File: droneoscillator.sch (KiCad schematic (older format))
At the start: 46 parts, among them J1 Conn_01x02, J2 Conn_01x03, Q1 BC337, Q2 BC337, Q3 BC337, Q4 BC337, U1 NE5532

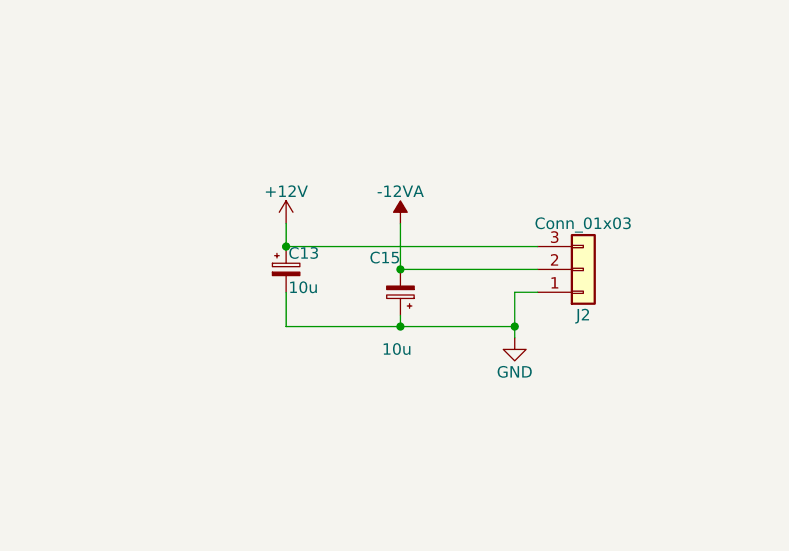
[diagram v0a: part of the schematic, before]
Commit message: added input filtering to power supply
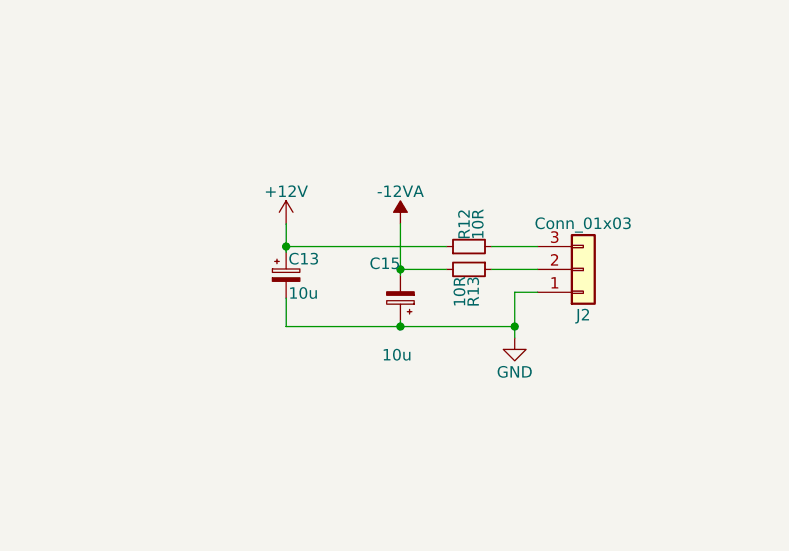
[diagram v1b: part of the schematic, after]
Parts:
- added R12, R13: 10R, Resistor_THT:R_Axial_DIN0204_L3.6mm_D1.6mm_P7.62mm_Horizontal, symbol droneoscillator-rescue:R_Small
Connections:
- net +12V: now also R12.1; no longer J2.3 (Pin_3)
- net -12VA: now also R13.2; no longer J2.2 (Pin_2)
- new net: J2.2 (Pin_2), R13.1
- new net: J2.3 (Pin_3), R12.2
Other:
- moved on the sheet: C13, C15
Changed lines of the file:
@@
 L droneoscillator-rescue:CP_Small C13
 U 1 1 5B2C205C
-P 8400 4700
-F 0 "C13" H 8410 4770 50  0000 L CNN
-F 1 "10u" H 8410 4620 50  0000 L CNN
-F 2 "Capacitor_THT:CP_Radial_D4.0mm_P2.00mm" H 8400 4700 50  0001 C CNN
-F 3 "" H 8400 4700 50  0001 C CNN
-	1    8400 4700
+P 8400 4725
+F 0 "C13" H 8410 4795 50  0000 L CNN
+F 1 "10u" H 8410 4645 50  0000 L CNN
+F 2 "Capacitor_THT:CP_Radial_D4.0mm_P2.00mm" H 8400 4725 50  0001 C CNN
+F 3 "" H 8400 4725 50  0001 C CNN
+	1    8400 4725
 	1    0    0    -1
 $EndComp
@@
 L droneoscillator-rescue:CP_Small C15
 U 1 1 5B2C2235
-P 8900 4800
-F 0 "C15" H 8900 4650 50  0000 L CNN
-F 1 "10u" H 8850 5050 50  0000 L CNN
-F 2 "Capacitor_THT:CP_Radial_D4.0mm_P2.00mm" H 8900 4800 50  0001 C CNN
-F 3 "" H 8900 4800 50  0001 C CNN
-	1    8900 4800
+P 8900 4825
+F 0 "C15" H 8900 4675 50  0000 L CNN
+F 1 "10u" H 8850 5075 50  0000 L CNN
+F 2 "Capacitor_THT:CP_Radial_D4.0mm_P2.00mm" H 8900 4825 50  0001 C CNN
+F 3 "" H 8900 4825 50  0001 C CNN
+	1    8900 4825
 	-1   0    0    1
 $EndComp
@@
 	9400 4800 9500 4800
 Wire Wire Line
-	8400 4800 8400 4950
+	8400 4825 8400 4950
 Connection ~ 9400 4950
-Connection ~ 8900 4700
-Connection ~ 8400 4600
-Wire Wire Line
-	8900 4950 8900 4900
+Wire Wire Line
+	8900 4950 8900 4925
 Connection ~ 8900 4950
 Wire Wire Line
@@
 	0    -1   -1   0
 $EndComp
-Wire Wire Line
-	8400 4600 9500 4600
-Wire Wire Line
-	8900 4700 9500 4700
+$Comp
+L droneoscillator-rescue:R_Small R12
+U 1 1 5C5321D3
+P 9200 4600
+F 0 "R12" H 9230 4620 50  0000 L CNN
+F 1 "10R" H 9230 4560 50  0000 L CNN
+F 2 "Resistor_THT:R_Axial_DIN0204_L3.6mm_D1.6mm_P7.62mm_Horizontal" H 9200 4600 50  0001 C CNN
+F 3 "" H 9200 4600 50  0001 C CNN
+	1    9200 4600
+	0    -1   -1   0
+$EndComp
+$Comp
+L droneoscillator-rescue:R_Small R13
+U 1 1 5C53254E
+P 9200 4700
+F 0 "R13" H 9230 4720 50  0000 L CNN
+F 1 "10R" H 9230 4660 50  0000 L CNN
+F 2 "Resistor_THT:R_Axial_DIN0204_L3.6mm_D1.6mm_P7.62mm_Horizontal" H 9200 4700 50  0001 C CNN
+F 3 "" H 9200 4700 50  0001 C CNN
+	1    9200 4700
+	0    1    1    0
+$EndComp
+Wire Wire Line
+	9500 4600 9300 4600
+Wire Wire Line
+	9100 4600 8400 4600
+Connection ~ 8400 4600
+Wire Wire Line
+	8400 4600 8400 4625
+Wire Wire Line
+	9300 4700 9500 4700
+Wire Wire Line
+	9100 4700 8900 4700
+Connection ~ 8900 4700
+Wire Wire Line
+	8900 4700 8900 4725
 $EndSCHEMATC

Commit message: pcb and schematic tweaks
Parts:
- RV5: value 100K -> 50K
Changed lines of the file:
@@
 P 2850 5150
 F 0 "RV5" V 2675 5150 50  0000 C CNN
-F 1 "100K" V 2750 5150 50  0000 C CNN
+F 1 "50K" V 2750 5150 50  0000 C CNN
 F 2 "Potentiometer_THT:Potentiometer_Alps_RK097_Single_Horizontal" H 2850 5150 50  0001 C CNN
 F 3 "" H 2850 5150 50  0001 C CNN
@@
 	2850 5000 2850 4950
 Wire Wire Line
-	2850 4950 3050 4950
-Wire Wire Line
-	3050 4950 3050 5150
-Wire Wire Line
-	3000 5150 3050 5150
-Wire Wire Line
 	3300 5150 3300 5250
-Connection ~ 3050 5150
 Connection ~ 3300 5150
 Wire Wire Line
@@
 Wire Wire Line
 	2650 5150 2700 5150
-Wire Wire Line
-	3050 5150 3300 5150
 Wire Wire Line
 	9450 1950 9450 2050
@@
 Wire Wire Line
 	8900 4700 8900 4725
+Connection ~ 3100 5150
+Wire Wire Line
+	3100 5150 3300 5150
+Wire Wire Line
+	3000 5150 3100 5150
+Wire Wire Line
+	2850 4950 3100 4950
+Wire Wire Line
+	3100 4950 3100 5150
 $EndSCHEMATC

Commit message: small tweaks, ready for sending to production
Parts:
- J1: value Conn_01x02 -> JST_XH_2
- J2: value Conn_01x03 -> JST_XH_3
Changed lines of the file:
@@
 U 1 1 5B23B79E
 P 2750 1750
-F 0 "RV1" H 2550 1800 50  0000 C CNN
-F 1 "50K" H 2550 1700 50  0000 C CNN
+F 0 "RV1" H 2625 1725 50  0000 C CNN
+F 1 "50K" H 2625 1800 50  0000 C CNN
 F 2 "Potentiometer_THT:Potentiometer_Alps_RK097_Single_Horizontal" H 2750 1750 50  0001 C CNN
 F 3 "" H 2750 1750 50  0001 C CNN
@@
 U 1 1 5B2BA8BE
 P 1400 5250
-F 0 "R4" H 1430 5270 50  0000 L CNN
-F 1 "10K" H 1430 5210 50  0000 L CNN
+F 0 "R4" V 1300 5175 50  0000 L CNN
+F 1 "10K" V 1350 5175 50  0000 L CNN
 F 2 "Resistor_THT:R_Axial_DIN0204_L3.6mm_D1.6mm_P7.62mm_Horizontal" H 1400 5250 50  0001 C CNN
 F 3 "" H 1400 5250 50  0001 C CNN
@@
 U 1 1 5B2BA9E5
 P 1400 4850
-F 0 "R2" H 1430 4870 50  0000 L CNN
-F 1 "10K" H 1430 4810 50  0000 L CNN
+F 0 "R2" V 1300 4775 50  0000 L CNN
+F 1 "10K" V 1350 4775 50  0000 L CNN
 F 2 "Resistor_THT:R_Axial_DIN0204_L3.6mm_D1.6mm_P7.62mm_Horizontal" H 1400 4850 50  0001 C CNN
 F 3 "" H 1400 4850 50  0001 C CNN
@@
 U 1 1 5B2BAA41
 P 1400 5050
-F 0 "R3" H 1430 5070 50  0000 L CNN
-F 1 "10K" H 1430 5010 50  0000 L CNN
+F 0 "R3" V 1300 4975 50  0000 L CNN
+F 1 "10K" V 1350 4975 50  0000 L CNN
 F 2 "Resistor_THT:R_Axial_DIN0204_L3.6mm_D1.6mm_P7.62mm_Horizontal" H 1400 5050 50  0001 C CNN
 F 3 "" H 1400 5050 50  0001 C CNN
@@
 U 1 1 5B2BADE9
 P 2500 5500
-F 0 "R5" H 2530 5520 50  0000 L CNN
-F 1 "56K" H 2530 5460 50  0000 L CNN
+F 0 "R5" V 2650 5425 50  0000 L CNN
+F 1 "56K" V 2575 5425 50  0000 L CNN
 F 2 "Resistor_THT:R_Axial_DIN0204_L3.6mm_D1.6mm_P7.62mm_Horizontal" H 2500 5500 50  0001 C CNN
 F 3 "" H 2500 5500 50  0001 C CNN
@@
 U 1 1 5B2BC3B3
 P 5100 1750
-F 0 "RV2" V 4925 1750 50  0000 C CNN
-F 1 "50K" V 5000 1750 50  0000 C CNN
+F 0 "RV2" H 4950 1725 50  0000 C CNN
+F 1 "50K" H 4950 1800 50  0000 C CNN
 F 2 "Potentiometer_THT:Potentiometer_Alps_RK097_Single_Horizontal" H 5100 1750 50  0001 C CNN
 F 3 "" H 5100 1750 50  0001 C CNN
@@
 P 5250 5350
 F 0 "J1" H 5250 5450 50  0000 C CNN
-F 1 "Conn_01x02" H 5250 5150 50  0000 C CNN
+F 1 "JST_XH_2" H 5250 5150 50  0000 C CNN
 F 2 "Connector_JST:JST_XH_B02B-XH-A_1x02_P2.50mm_Vertical" H 5250 5350 50  0001 C CNN
 F 3 "" H 5250 5350 50  0001 C CNN
@@
 U 1 1 5B2C0BFD
 P 1400 4650
-F 0 "R9" H 1430 4670 50  0000 L CNN
-F 1 "10K" H 1430 4610 50  0000 L CNN
+F 0 "R9" V 1300 4575 50  0000 L CNN
+F 1 "10K" V 1350 4575 50  0000 L CNN
 F 2 "Resistor_THT:R_Axial_DIN0204_L3.6mm_D1.6mm_P7.62mm_Horizontal" H 1400 4650 50  0001 C CNN
 F 3 "" H 1400 4650 50  0001 C CNN
@@
 P 9700 4700
 F 0 "J2" H 9700 4900 50  0000 C CNN
-F 1 "Conn_01x03" H 9700 4500 50  0000 C CNN
+F 1 "JST_XH_3" H 9700 4500 50  0000 C CNN
 F 2 "Connector_JST:JST_XH_B03B-XH-A_1x03_P2.50mm_Vertical" H 9700 4700 50  0001 C CNN
 F 3 "" H 9700 4700 50  0001 C CNN
@@
 U 1 1 5B2C205C
 P 8400 4725
-F 0 "C13" H 8410 4795 50  0000 L CNN
-F 1 "10u" H 8410 4645 50  0000 L CNN
+F 0 "C13" H 8175 4775 50  0000 L CNN
+F 1 "10u" H 8175 4700 50  0000 L CNN
 F 2 "Capacitor_THT:CP_Radial_D4.0mm_P2.00mm" H 8400 4725 50  0001 C CNN
 F 3 "" H 8400 4725 50  0001 C CNN
@@
 U 1 1 5B2C2235
 P 8900 4825
-F 0 "C15" H 8900 4675 50  0000 L CNN
-F 1 "10u" H 8850 5075 50  0000 L CNN
+F 0 "C15" H 8975 4800 50  0000 L CNN
+F 1 "10u" H 8975 4900 50  0000 L CNN
 F 2 "Capacitor_THT:CP_Radial_D4.0mm_P2.00mm" H 8900 4825 50  0001 C CNN
 F 3 "" H 8900 4825 50  0001 C CNN
@@
 U 1 1 5C2FDC7E
 P 3100 1950
-F 0 "R6" H 3130 1970 50  0000 L CNN
-F 1 "10K" H 3130 1910 50  0000 L CNN
+F 0 "R6" V 2950 1875 50  0000 L CNN
+F 1 "10K" V 3025 1875 50  0000 L CNN
 F 2 "Resistor_THT:R_Axial_DIN0204_L3.6mm_D1.6mm_P7.62mm_Horizontal" H 3100 1950 50  0001 C CNN
 F 3 "" H 3100 1950 50  0001 C CNN
@@
 U 1 1 5C30BE71
 P 5450 1950
-F 0 "R14" H 5480 1970 50  0000 L CNN
-F 1 "10K" H 5480 1910 50  0000 L CNN
+F 0 "R14" V 5300 1900 50  0000 L CNN
+F 1 "10K" V 5375 1900 50  0000 L CNN
 F 2 "Resistor_THT:R_Axial_DIN0204_L3.6mm_D1.6mm_P7.62mm_Horizontal" H 5450 1950 50  0001 C CNN
 F 3 "" H 5450 1950 50  0001 C CNN
@@
 U 1 1 5C31A005
 P 7600 1950
-F 0 "R16" H 7630 1970 50  0000 L CNN
-F 1 "10K" H 7630 1910 50  0000 L CNN
+F 0 "R16" V 7450 1875 50  0000 L CNN
+F 1 "10K" V 7525 1875 50  0000 L CNN
 F 2 "Resistor_THT:R_Axial_DIN0204_L3.6mm_D1.6mm_P7.62mm_Horizontal" H 7600 1950 50  0001 C CNN
 F 3 "" H 7600 1950 50  0001 C CNN
@@
 U 1 1 5C32CF45
 P 9800 1950
-F 0 "R18" H 9830 1970 50  0000 L CNN
-F 1 "10K" H 9830 1910 50  0000 L CNN
+F 0 "R18" V 9650 1875 50  0000 L CNN
+F 1 "10K" V 9725 1875 50  0000 L CNN
 F 2 "Resistor_THT:R_Axial_DIN0204_L3.6mm_D1.6mm_P7.62mm_Horizontal" H 9800 1950 50  0001 C CNN
 F 3 "" H 9800 1950 50  0001 C CNN
@@
 U 1 1 5C4614EE
 P 3350 1950
-F 0 "C3" H 3360 2020 50  0000 L CNN
-F 1 "2u2" H 3360 1870 50  0000 L CNN
+F 0 "C3" V 3525 1925 50  0000 L CNN
+F 1 "2u2" V 3450 1875 50  0000 L CNN
 F 2 "Capacitor_THT:CP_Radial_D4.0mm_P2.00mm" H 3350 1950 50  0001 C CNN
 F 3 "" H 3350 1950 50  0001 C CNN
@@
 U 1 1 5C46AFD2
 P 5700 1950
-F 0 "C6" H 5710 2020 50  0000 L CNN
-F 1 "2u2" H 5710 1870 50  0000 L CNN
+F 0 "C6" V 5875 1875 50  0000 L CNN
+F 1 "2u2" V 5800 1875 50  0000 L CNN
 F 2 "Capacitor_THT:CP_Radial_D4.0mm_P2.00mm" H 5700 1950 50  0001 C CNN
 F 3 "" H 5700 1950 50  0001 C CNN
@@
 U 1 1 5C46B279
 P 7850 1950
-F 0 "C7" H 7860 2020 50  0000 L CNN
-F 1 "2u2" H 7860 1870 50  0000 L CNN
+F 0 "C7" V 8025 1925 50  0000 L CNN
+F 1 "2u2" V 7950 1875 50  0000 L CNN
 F 2 "Capacitor_THT:CP_Radial_D4.0mm_P2.00mm" H 7850 1950 50  0001 C CNN
 F 3 "" H 7850 1950 50  0001 C CNN
@@
 U 1 1 5C46B4C7
 P 10050 1950
-F 0 "C9" H 10060 2020 50  0000 L CNN
-F 1 "2u2" H 10060 1870 50  0000 L CNN
+F 0 "C9" V 10225 1900 50  0000 L CNN
+F 1 "2u2" V 10150 1900 50  0000 L CNN
 F 2 "Capacitor_THT:CP_Radial_D4.0mm_P2.00mm" H 10050 1950 50  0001 C CNN
 F 3 "" H 10050 1950 50  0001 C CNN
@@
 U 1 1 5C5321D3
 P 9200 4600
-F 0 "R12" H 9230 4620 50  0000 L CNN
-F 1 "10R" H 9230 4560 50  0000 L CNN
+F 0 "R12" V 9350 4525 50  0000 L CNN
+F 1 "10R" V 9275 4525 50  0000 L CNN
 F 2 "Resistor_THT:R_Axial_DIN0204_L3.6mm_D1.6mm_P7.62mm_Horizontal" H 9200 4600 50  0001 C CNN
 F 3 "" H 9200 4600 50  0001 C CNN
@@
 U 1 1 5C53254E
 P 9200 4700
-F 0 "R13" H 9230 4720 50  0000 L CNN
-F 1 "10R" H 9230 4660 50  0000 L CNN
+F 0 "R13" V 9275 4625 50  0000 L CNN
+F 1 "10R" V 9350 4625 50  0000 L CNN
 F 2 "Resistor_THT:R_Axial_DIN0204_L3.6mm_D1.6mm_P7.62mm_Horizontal" H 9200 4700 50  0001 C CNN
 F 3 "" H 9200 4700 50  0001 C CNN

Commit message: Minor BOM adjustments
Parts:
- C15: Notes (none) -> <6mm height required
- Q1, Q2, Q3, Q4: Notes (none) -> Cut middle leg flush with case
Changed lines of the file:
@@
 F 2 "Package_TO_SOT_THT:TO-92_Inline_Wide" H 2850 2175 50  0001 L CIN
 F 3 "" H 2650 2250 50  0001 L CNN
+F 4 "Cut middle leg flush with case" H 2650 2250 50  0001 C CNN "Notes"
 	1    2650 2250
 	1    0    0    1
@@
 $EndComp
 $Comp
-L droneoscillator-rescue:BC337 Q2
-U 1 1 5B2B7413
-P 5000 2250
-F 0 "Q2" H 5200 2325 50  0000 L CNN
-F 1 "BC337" H 5200 2250 50  0000 L CNN
-F 2 "Package_TO_SOT_THT:TO-92_Inline_Wide" H 5200 2175 50  0001 L CIN
-F 3 "" H 5000 2250 50  0001 L CNN
-	1    5000 2250
-	1    0    0    1
-$EndComp
-$Comp
 L droneoscillator-rescue:R_Small R7
 U 1 1 5B2B7419
@@
 $EndComp
 $Comp
-L droneoscillator-rescue:BC337 Q3
-U 1 1 5B2B7643
-P 7150 2250
-F 0 "Q3" H 7350 2325 50  0000 L CNN
-F 1 "BC337" H 7350 2250 50  0000 L CNN
-F 2 "Package_TO_SOT_THT:TO-92_Inline_Wide" H 7350 2175 50  0001 L CIN
-F 3 "" H 7150 2250 50  0001 L CNN
-	1    7150 2250
-	1    0    0    1
-$EndComp
-$Comp
 L droneoscillator-rescue:R_Small R8
 U 1 1 5B2B7649
@@
 $EndComp
 $Comp
-L droneoscillator-rescue:BC337 Q4
-U 1 1 5B2C0B2C
-P 9350 2250
-F 0 "Q4" H 9550 2325 50  0000 L CNN
-F 1 "BC337" H 9550 2250 50  0000 L CNN
-F 2 "Package_TO_SOT_THT:TO-92_Inline_Wide" H 9550 2175 50  0001 L CIN
-F 3 "" H 9350 2250 50  0001 L CNN
-	1    9350 2250
-	1    0    0    1
-$EndComp
-$Comp
 L droneoscillator-rescue:R_Small R10
 U 1 1 5B2C0B32
@@
 F 2 "Capacitor_THT:CP_Radial_D4.0mm_P2.00mm" H 8900 4825 50  0001 C CNN
 F 3 "" H 8900 4825 50  0001 C CNN
+F 4 "<6mm height required" H 8900 4825 50  0001 C CNN "Notes"
 	1    8900 4825
 	-1   0    0    1
@@
 Wire Wire Line
 	3100 4950 3100 5150
+$Comp
+L droneoscillator-rescue:BC337 Q2
+U 1 1 5C6C6EE0
+P 5000 2250
+F 0 "Q2" H 5200 2325 50  0000 L CNN
+F 1 "BC337" H 5200 2250 50  0000 L CNN
+F 2 "Package_TO_SOT_THT:TO-92_Inline_Wide" H 5200 2175 50  0001 L CIN
+F 3 "" H 5000 2250 50  0001 L CNN
+F 4 "Cut middle leg flush with case" H 5000 2250 50  0001 C CNN "Notes"
+	1    5000 2250
+	1    0    0    1
+$EndComp
+$Comp
+L droneoscillator-rescue:BC337 Q3
+U 1 1 5C6C7285
+P 7150 2250
+F 0 "Q3" H 7350 2325 50  0000 L CNN
+F 1 "BC337" H 7350 2250 50  0000 L CNN
+F 2 "Package_TO_SOT_THT:TO-92_Inline_Wide" H 7350 2175 50  0001 L CIN
+F 3 "" H 7150 2250 50  0001 L CNN
+F 4 "Cut middle leg flush with case" H 7150 2250 50  0001 C CNN "Notes"
+	1    7150 2250
+	1    0    0    1
+$EndComp
+$Comp
+L droneoscillator-rescue:BC337 Q4
+U 1 1 5C6C7309
+P 9350 2250
+F 0 "Q4" H 9550 2325 50  0000 L CNN
+F 1 "BC337" H 9550 2250 50  0000 L CNN
+F 2 "Package_TO_SOT_THT:TO-92_Inline_Wide" H 9550 2175 50  0001 L CIN
+F 3 "" H 9350 2250 50  0001 L CNN
+F 4 "Cut middle leg flush with case" H 9350 2250 50  0001 C CNN "Notes"
+	1    9350 2250
+	1    0    0    1
+$EndComp
 $EndSCHEMATC

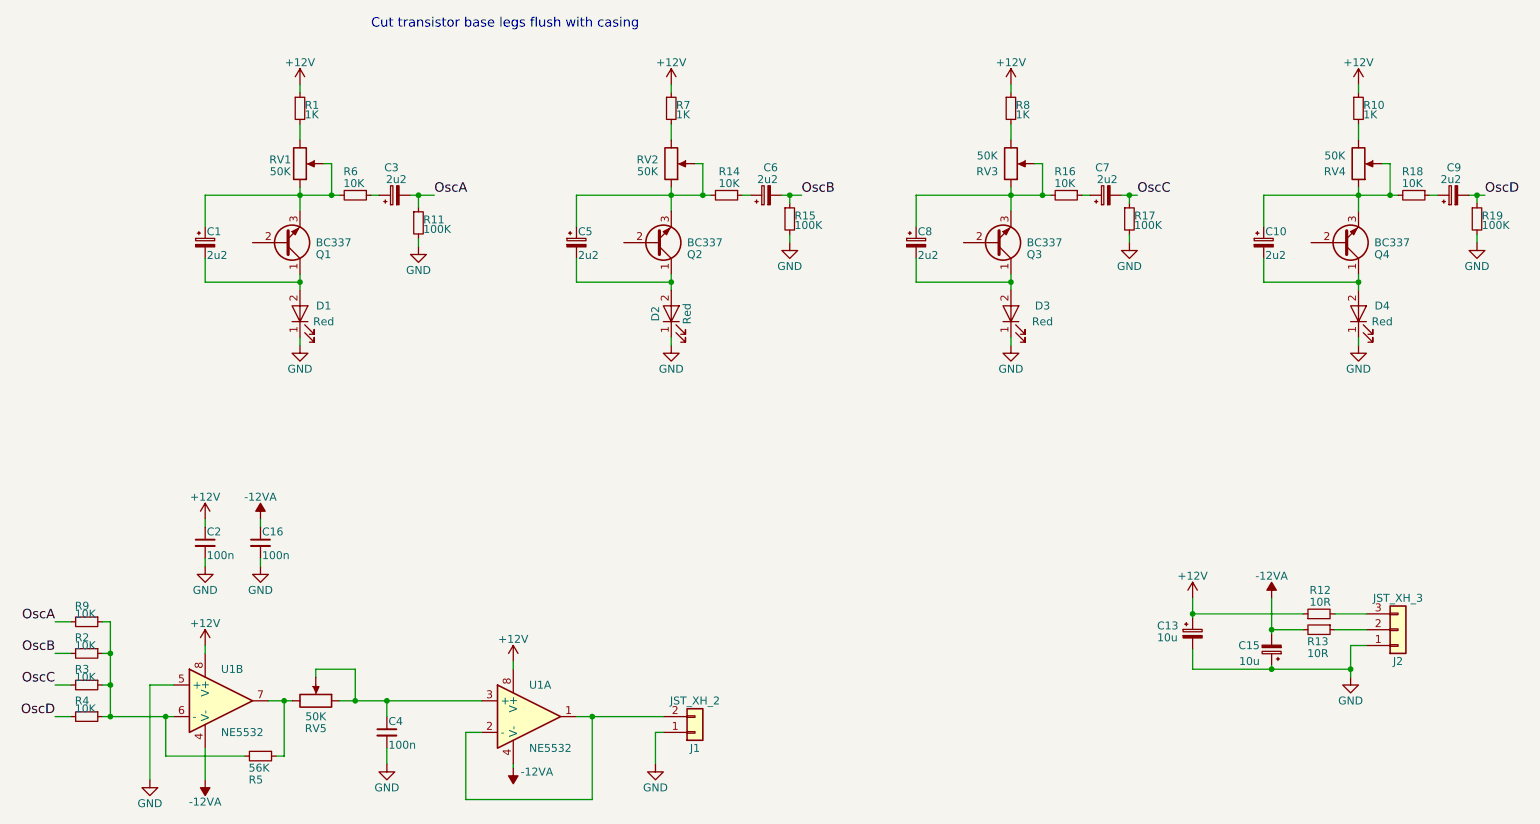
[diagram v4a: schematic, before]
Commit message: updated BOM + component notes
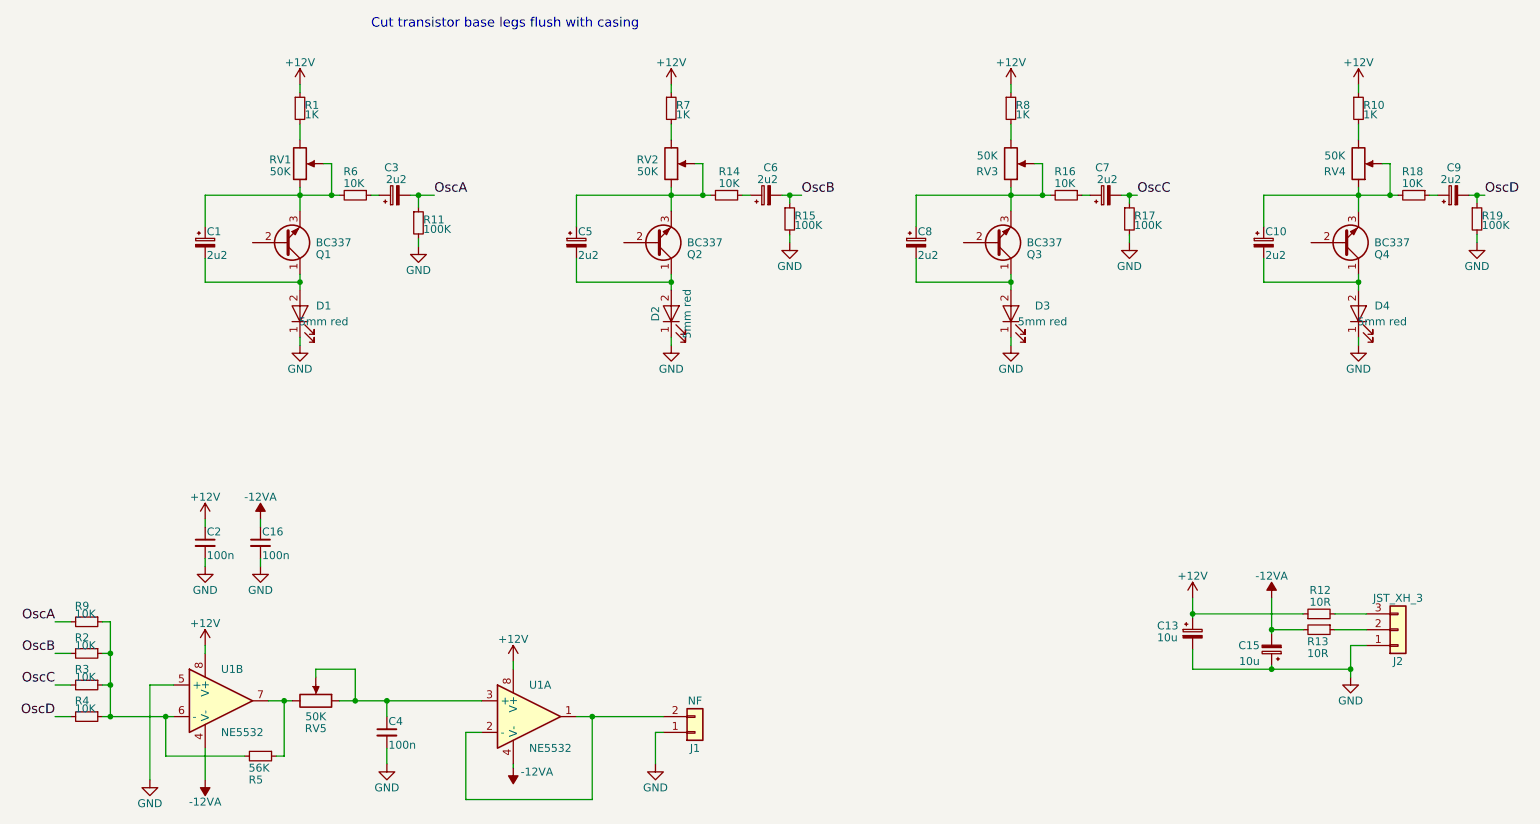
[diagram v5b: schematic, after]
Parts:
- D1, D2, D3, D4: value Red -> 5mm red
- J1: value JST_XH_2 -> NF
- RV1, RV2, RV3, RV4: Notes (none) -> Alps RK097 series or equivalent
- U1: Notes (none) -> Can be subsituted for other standard dual op-amp (TL074, LM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
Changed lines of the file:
@@
 F 2 "Potentiometer_THT:Potentiometer_Alps_RK097_Single_Horizontal" H 2750 1750 50  0001 C CNN
 F 3 "" H 2750 1750 50  0001 C CNN
+F 4 "Alps RK097 series or equivalent" H 2750 1750 50  0001 C CNN "Notes"
 	1    2750 1750
 	1    0    0    1
@@
 P 2750 2700
 F 0 "D1" V 2800 2550 50  0000 C CNN
-F 1 "Red" V 2700 2550 50  0000 C CNN
+F 1 "5mm red" V 2700 2550 50  0000 C CNN
 F 2 "LED_THT:LED_D5.0mm_Horizontal_O1.27mm_Z3.0mm" H 2750 2700 50  0001 C CNN
 F 3 "" H 2750 2700 50  0001 C CNN
@@
 F 2 "Potentiometer_THT:Potentiometer_Alps_RK097_Single_Horizontal" H 7250 1750 50  0001 C CNN
 F 3 "" H 7250 1750 50  0001 C CNN
+F 4 "Alps RK097 series or equivalent" H 7250 1750 50  0001 C CNN "Notes"
 	1    7250 1750
 	1    0    0    1
@@
 P 5100 2700
 F 0 "D2" H 5100 2800 50  0000 C CNN
-F 1 "Red" H 5100 2600 50  0000 C CNN
+F 1 "5mm red" H 5100 2600 50  0000 C CNN
 F 2 "LED_THT:LED_D5.0mm_Horizontal_O1.27mm_Z3.0mm" H 5100 2700 50  0001 C CNN
 F 3 "" H 5100 2700 50  0001 C CNN
@@
 F 2 "Potentiometer_THT:Potentiometer_Alps_RK097_Single_Horizontal" H 9450 1750 50  0001 C CNN
 F 3 "" H 9450 1750 50  0001 C CNN
+F 4 "Alps RK097 series or equivalent" H 9450 1750 50  0001 C CNN "Notes"
 	1    9450 1750
 	1    0    0    1
@@
 P 7250 2700
 F 0 "D3" V 7300 2500 50  0000 C CNN
-F 1 "Red" V 7200 2500 50  0000 C CNN
+F 1 "5mm red" V 7200 2500 50  0000 C CNN
 F 2 "LED_THT:LED_D5.0mm_Horizontal_O1.27mm_Z3.0mm" H 7250 2700 50  0001 C CNN
 F 3 "" H 7250 2700 50  0001 C CNN
@@
 F 2 "Potentiometer_THT:Potentiometer_Alps_RK097_Single_Horizontal" H 5100 1750 50  0001 C CNN
 F 3 "" H 5100 1750 50  0001 C CNN
+F 4 "Alps RK097 series or equivalent" H 5100 1750 50  0001 C CNN "Notes"
 	1    5100 1750
 	1    0    0    1
@@
 F 2 "Package_DIP:DIP-8_W7.62mm_Socket_LongPads" H 2250 5150 50  0001 C CNN
 F 3 "" H 2250 5150 50  0001 C CNN
+F 4 "Can be subsituted for other standard dual op-amp (TL074, LM358, RC4580 etc)" H 2250 5150 50  0001 C CNN "Notes"
 	2    2250 5150
 	1    0    0    -1
@@
 P 5250 5350
 F 0 "J1" H 5250 5450 50  0000 C CNN
-F 1 "JST_XH_2" H 5250 5150 50  0000 C CNN
+F 1 "NF" H 5250 5150 50  0000 C CNN
 F 2 "Connector_JST:JST_XH_B02B-XH-A_1x02_P2.50mm_Vertical" H 5250 5350 50  0001 C CNN
 F 3 "" H 5250 5350 50  0001 C CNN
@@
 P 9450 2700
 F 0 "D4" V 9500 2550 50  0000 C CNN
-F 1 "Red" V 9400 2550 50  0000 C CNN
+F 1 "5mm red" V 9400 2550 50  0000 C CNN
 F 2 "LED_THT:LED_D5.0mm_Horizontal_O1.27mm_Z3.0mm" H 9450 2700 50  0001 C CNN
 F 3 "" H 9450 2700 50  0001 C CNN
